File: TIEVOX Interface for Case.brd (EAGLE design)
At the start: 63.9 x 80 mm, 23 parts, among them IC1 DMMT5401, Q1 DMP2305U-7, U4 CAT24C32.UDFN8

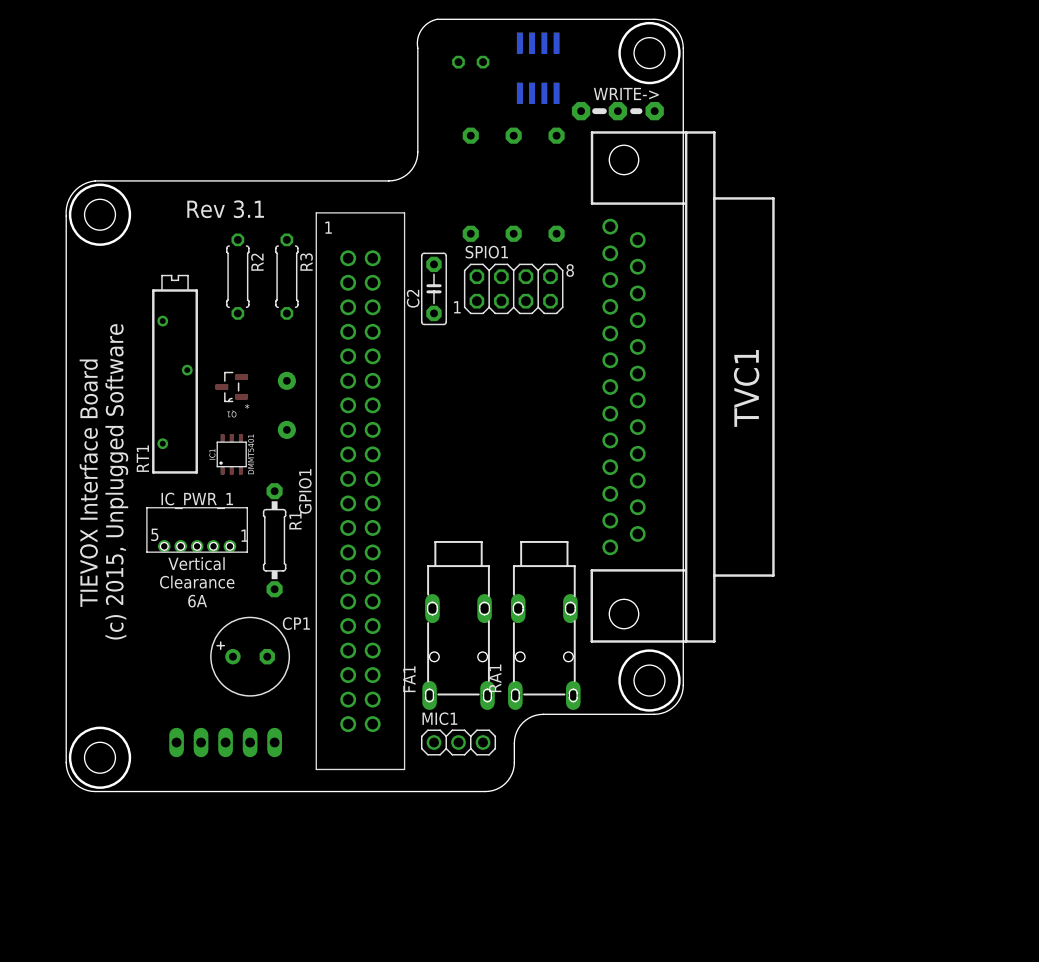
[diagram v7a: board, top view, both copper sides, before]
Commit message: Should have working versions of all required boards now.
Updated to No Commercial license.
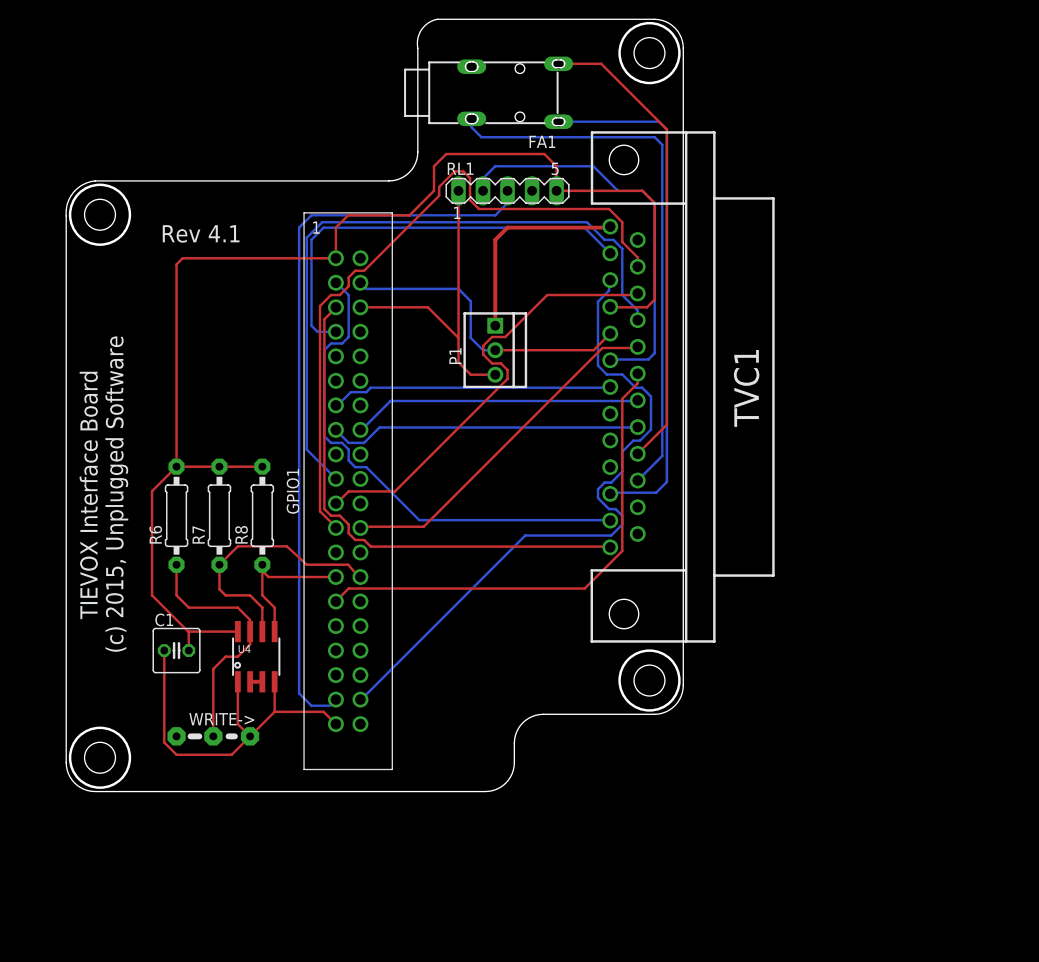
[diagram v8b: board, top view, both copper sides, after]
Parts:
- removed C2: 0.1uf, capacitor-wima:C5B2.5
- removed CP1: 1000uF, rcl:E3,5-8
- removed F1: 06R155BPR, SparkFun-PowerIC:PTC
- removed IC1: DMMT5401, Diodes_Inc_By_element14_Batch_1:DMMT5401
- removed IC_PWR_1: 6A, packages:NE12S
- removed MIC1: (no value), adafruit:1X03
- removed Q1: DMP2305U-7, Diodes_Inc_By_element14_Batch_1:SOT103P240X110-3N
- removed R1: 2.2K, adafruit:0207/10
- removed R2: 10K, 1%, adafruit:0207/7
- removed R3: 47K, 1%, adafruit:0207/7
- removed RA1: 1503_07, con-lumberg:1503_07
- removed RT1: 10K, resistor:RTRIM3006P
- removed SPIO1: 2.4GHz, pinhead:2X04
- added P1: Power, connector:PINHEAD-LOCK-3
- moved WRITE-> 77.1 mm to (13.3, 5.71)
- moved C1 68.2 mm to (11.4, 14.6), flipped to the top
- moved U4 67.6 mm to (19.7, 14.0), flipped to the top, turned to 0 degrees
- moved RL1 64.2 mm to (45.7, 62.2), flipped to the top
- moved FA1 51.4 mm to (40.0, 72.4), turned to 90 degrees
- moved R6 48.9 mm to (11.4, 28.6), flipped to the top, turned to 90 degrees
- moved R8 45.9 mm to (20.3, 28.6), flipped to the top, turned to 90 degrees
- moved R7 43.1 mm to (15.9, 28.6), flipped to the top, turned to 90 degrees
- moved GPIO1 1.27 mm to (29.2, 31.1)
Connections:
- removed net IN: F1.P$2, IC1.E1, Q1.3
- removed net N$11: GPIO1.31_GPIO6, SPIO1.8
- removed net N$12: RA1.2@1, TVC1.SOUND_RR
- removed net N$13: RA1.3, TVC1.SOUND_RL
- removed net N$16: MIC1.1, TVC1.MIC_IN
- removed net N$17: MIC1.2, TVC1.MIC_COMMON
- removed net N$22: GPIO1.35_GPIO19, MIC1.3
- removed net N$28: CP1.+, F1.P$1, IC_PWR_1.VOUT
- removed net N$29: IC_PWR_1.ENABLE, R1.2
- removed net N$32: IC1.B1, IC1.B2, IC1.C1, R2.2
- removed net N$33: IC1.C2, Q1.1, R3.2
- removed net N$4: GPIO1.22_GPIO25, SPIO1.3
- removed net N$6: RA1.1, TVC1.REAR_COMMON
- removed net N$7: GPIO1.26_SPI0_CE1, SPIO1.4
- removed net PWR12_TRIM: IC_PWR_1.TRIM, RT1.2
- new net 14_GND: GPIO1.14_GND
- new net 17_3.3VDC: GPIO1.17_3.3VDC
- new net 20_GND: GPIO1.20_GND
- new net 25_GND: GPIO1.25_GND
- new net 2_5VDC: GPIO1.2_5VDC
- new net 30_GND: GPIO1.30_GND
- new net 9_GND: GPIO1.9_GND
- new net GND_39: C1.1, GPIO1.39_GND, U4.1, U4.4, WRITE->.3
- net +3.3VDC: no longer C2.2, GPIO1.17_3.3VDC, SPIO1.2
- net +5VDC: now also P1.2; no longer GPIO1.2_5VDC, IC1.E2, Q1.2
- net GND: now also P1.3; no longer C1.1, C2.1, CP1.-, GPIO1.14_GND, GPIO1.20_GND, GPIO1.25_GND, GPIO1.30_GND, GPIO1.39_GND, GPIO1.9_GND, IC_PWR_1.GND, R1.1, R2.1, R3.1, RT1.1, SPIO1.1, TVC1.GND, U4.1, U4.4, WRITE->.3
- net N$10: no longer SPIO1.6
- net N$31: now also GPIO1.37_GPIO26
- net N$8: no longer SPIO1.5
- net N$9: no longer SPIO1.7
- net PWR12_IN: now also P1.1; no longer IC_PWR_1.VIN
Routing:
- net +3.3VDC: track 0.00 -> 132.8 mm
- net N$31: track 0.00 -> 76.8 mm
- net N$8: track 0.00 -> 70.6 mm
- net N$10: track 0.00 -> 68.8 mm
- net N$25: track 0.00 -> 68.6 mm
- net N$14: track 0.00 -> 57.2 mm
- net N$5: track 0.00 -> 54.5 mm
- net N$18: track 0.00 -> 53.2 mm
- net N$19: track 0.00 -> 52.1 mm
- net N$26: track 0.00 -> 50.9 mm
- net N$15: track 0.00 -> 48.9 mm
- net N$9: track 0.00 -> 46.5 mm
- net N$24: track 0.00 -> 44.3 mm
- net N$21: track 0.00 -> 41.6 mm
- net GND_39: track 0.00 -> 39.5 mm
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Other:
- board text added: "Rev 4.1"
- board text removed: "Rev 3.1"
